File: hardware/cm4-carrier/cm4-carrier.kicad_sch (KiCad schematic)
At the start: 0 parts

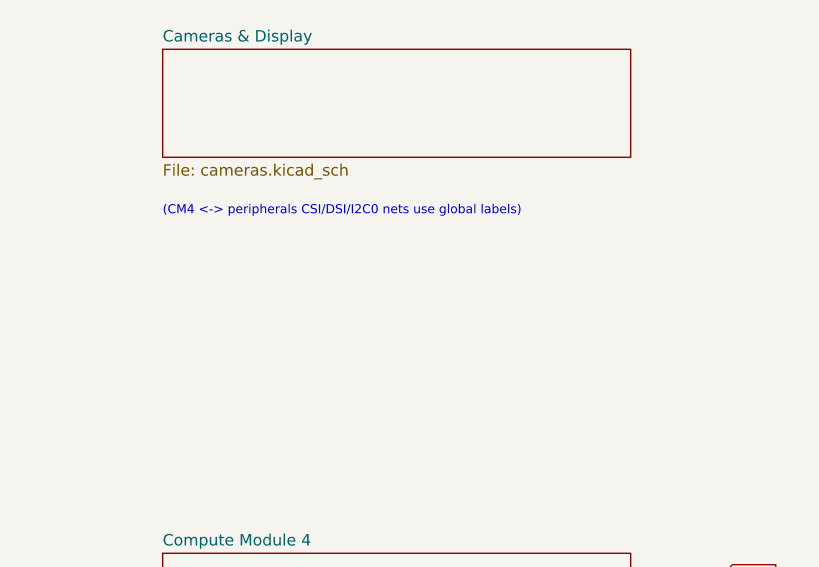
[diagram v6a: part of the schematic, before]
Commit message: Add microSD boot (CM4 Lite) and CM4 bring-up controls
Add a boot_sd.kicad_sch sub-sheet with a microSD socket and the CM4 module
bring-up controls, so a CM4 Lite (no eMMC) can boot from card:

- microSD socket (J8, Hirose DM3D-SF) wired to the CM4 SD interface
  (SD_CLK/SD_CMD/SD_DAT0-3) with CMD/DAT pull-ups and a card-detect pull-up.
- SD 3.3V is gated by a high-side load switch (Q2 P-FET + Q3 N-FET) driven by
  the CM4's SD_PWR_ON (active high), with the card rail decoupled (C16/C17).
  SD_VDD_Override is defaulted low (3.3V card).
- Bring-up controls: GLOBAL_EN (power/enable, SW1), RUN_PG (run/reset, SW2)
  and nRPIBOOT (USB/rpiboot, SW3), each with a pull-up and momentary button;
  nEXTRST pulled up; power/activity LEDs (D3/D4) on PI_LED_nPWR / PI_LED_ACT.

The CM4 sheet now exports the SD interface and the GLOBAL_EN/RUN_PG/nRPIBOOT/
nEXTRST/PI_LED/SD_PWR_ON/SD_VDD_Override pins (from J1) as global nets; the
boot sheet consumes them. Pin directions were taken from the CM4 pin map;
microSD/SOT-23/tact-switch footprints from KiCad libraries.

Root gains a (pinless) Boot sheet box (page 8, now 7 sub-sheets). README/BOM
updated. No format change (KiCad 10, 20260306).

Co-Authored-By: Claude Opus 4.8 <noreply@anthropic.com>
Claude-Session: https://claude.ai/code/session_015B7X7FE461jFSRaiTFdnFt
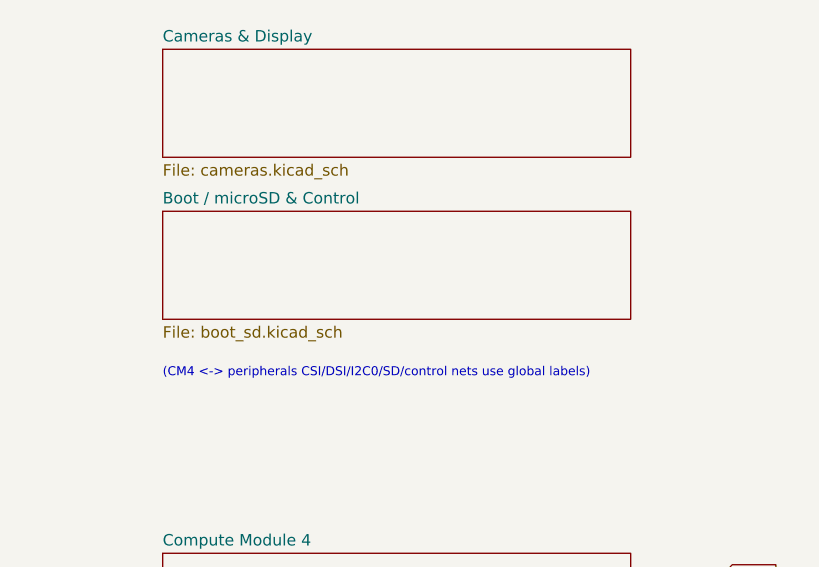
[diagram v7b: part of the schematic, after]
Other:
- added sheet Boot / microSD & Control (boot_sd.kicad_sch)
- note added: "(CM4 <-> peripherals CSI/DSI/I2C0/SD/control nets use global labels)"
- note removed: "(CM4 <-> peripherals CSI/DSI/I2C0 nets use global labels)"
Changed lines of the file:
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@@
 		(instances
 			(project "cm4-carrier"
-				(path "/68164e39-daeb-4d86-8c19-ac7cd09b1aca"
+				(path "/c714cb6b-329f-4585-a26c-317da9f46ca5"
 					(page "6"))))
 	)
@@
 		(instances
 			(project "cm4-carrier"
-				(path "/68164e39-daeb-4d86-8c19-ac7cd09b1aca"
+				(path "/c714cb6b-329f-4585-a26c-317da9f46ca5"
 					(page "2"))))
 	)
@@
 		(instances
 			(project "cm4-carrier"
-				(path "/68164e39-daeb-4d86-8c19-ac7cd09b1aca"
+				(path "/c714cb6b-329f-4585-a26c-317da9f46ca5"
 					(page "3"))))
 	)
@@
 		(instances
 			(project "cm4-carrier"
-				(path "/68164e39-daeb-4d86-8c19-ac7cd09b1aca"
+				(path "/c714cb6b-329f-4585-a26c-317da9f46ca5"
 					(page "4"))))
 	)
@@
 		(instances
 			(project "cm4-carrier"
-				(path "/68164e39-daeb-4d86-8c19-ac7cd09b1aca"
+				(path "/c714cb6b-329f-4585-a26c-317da9f46ca5"
 					(page "5"))))
 	)
@@
 		(instances
 			(project "cm4-carrier"
-				(path "/68164e39-daeb-4d86-8c19-ac7cd09b1aca"
+				(path "/c714cb6b-329f-4585-a26c-317da9f46ca5"
 					(page "7"))))
 	)
-	(text "(CM4 <-> peripherals CSI/DSI/I2C0 nets use global labels)" (at 155.00 58.00 0)
+	(sheet (at 155.00 58.00) (size 52.00 12.00)
+		(exclude_from_sim no) (in_bom yes) (on_board yes) (dnp no)
+		(fields_autoplaced yes)
+		(stroke (width 0.1524) (type solid))
+		(fill (color 0 0 0 0.0000))
+		(property "Sheetname" "Boot / microSD & Control" (at 155.00 57.29 0)
+			(effects (font (size 1.27 1.27)) (justify left bottom)))
+		(property "Sheetfile" "boot_sd.kicad_sch" (at 155.00 70.71 0)
+			(effects (font (size 1.27 1.27)) (justify left top)))
+		(instances
+			(project "cm4-carrier"
+				(path "/c714cb6b-329f-4585-a26c-317da9f46ca5"
+					(page "8"))))
+	)
+	(text "(CM4 <-> peripherals CSI/DSI/I2C0/SD/control nets use global labels)" (at 155.00 76.00 0)
 		(effects (font (size 1.0 1.0)) (justify left))
 )

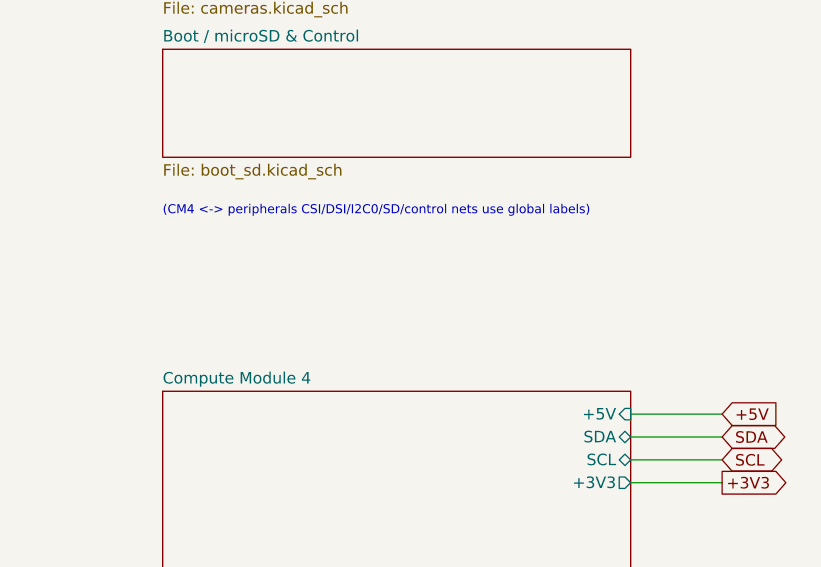
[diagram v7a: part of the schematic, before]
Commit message: Add stereo I2S audio (2x ICS-43434 mics + 2x MAX98357A amps)
Add an audio.kicad_sch sub-sheet with stereo microphone capture and stereo
speaker output over the CM4's I2S peripheral:

- 2x ICS-43434 I2S MEMS mics (U8 Left = LR->GND, U9 Right = LR->VDD) sharing
  the I2S RX bus, powered at 3.3V, with decoupling.
- 2x MAX98357A I2S class-D amps (U10 Left, U11 Right) on the I2S TX bus,
  powered at 5V; channel selected by the SD_MODE resistor divider, GAIN_SLOT
  set via 100k, VDD bulk/decoupling. Filterless BTL outputs go straight to the
  speaker connector.
- 4-pin 1.25mm (JST GH) speaker connector J9 = SPK_L+/L-/R+/R-.

The CM4 sheet exports the I2S bus (GPIO18=BCLK, GPIO19=LRCLK, GPIO20=PCM_DIN,
GPIO21=PCM_DOUT) as global nets I2S_CLK/FS/DIN/DOUT; the audio sheet consumes
them. Both mics+amps share BCLK/LRCLK; mics drive DIN, amps receive DOUT.

Pinouts: ICS-43434 from KiCad Sensor_Audio; MAX98357A (TQFN-16) from KiCad
symbol MR !3846; JST GH 4-pin footprint from KiCad. Root gains a (pinless)
Stereo Audio box (page 9, now 8 sub-sheets). README/BOM updated. No format
change (KiCad 10, 20260306).

Co-Authored-By: Claude Opus 4.8 <noreply@anthropic.com>
Claude-Session: https://claude.ai/code/session_015B7X7FE461jFSRaiTFdnFt
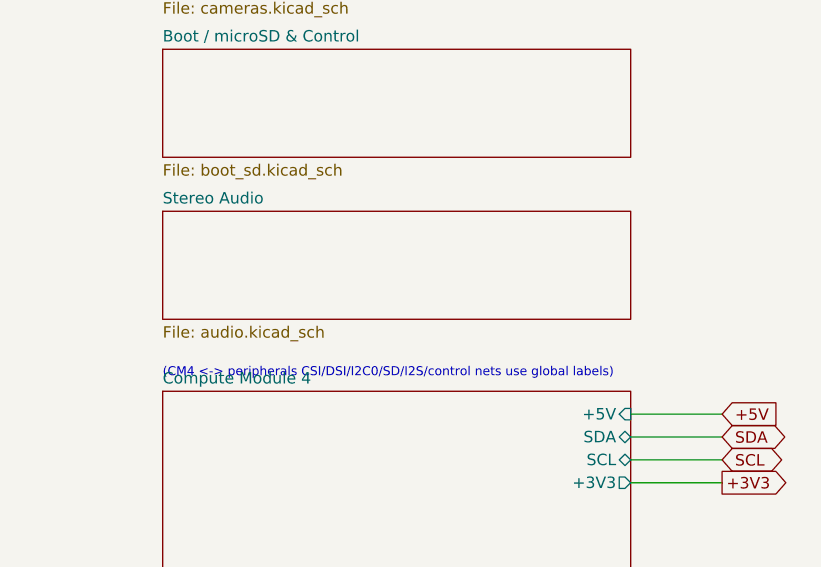
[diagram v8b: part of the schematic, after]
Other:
- added sheet Stereo Audio (audio.kicad_sch)
- note added: "(CM4 <-> peripherals CSI/DSI/I2C0/SD/I2S/control nets use global labels)"
- note removed: "(CM4 <-> peripherals CSI/DSI/I2C0/SD/control nets use global labels)"
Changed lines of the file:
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@@
 		(instances
 			(project "cm4-carrier"
-				(path "/c714cb6b-329f-4585-a26c-317da9f46ca5"
+				(path "/4125949c-82e9-47d9-b22c-a43e01f07343"
 					(page "6"))))
 	)
@@
 		(instances
 			(project "cm4-carrier"
-				(path "/c714cb6b-329f-4585-a26c-317da9f46ca5"
+				(path "/4125949c-82e9-47d9-b22c-a43e01f07343"
 					(page "2"))))
 	)
@@
 		(instances
 			(project "cm4-carrier"
-				(path "/c714cb6b-329f-4585-a26c-317da9f46ca5"
+				(path "/4125949c-82e9-47d9-b22c-a43e01f07343"
 					(page "3"))))
 	)
@@
 		(instances
 			(project "cm4-carrier"
-				(path "/c714cb6b-329f-4585-a26c-317da9f46ca5"
+				(path "/4125949c-82e9-47d9-b22c-a43e01f07343"
 					(page "4"))))
 	)
@@
 		(instances
 			(project "cm4-carrier"
-				(path "/c714cb6b-329f-4585-a26c-317da9f46ca5"
+				(path "/4125949c-82e9-47d9-b22c-a43e01f07343"
 					(page "5"))))
 	)
@@
 		(instances
 			(project "cm4-carrier"
-				(path "/c714cb6b-329f-4585-a26c-317da9f46ca5"
+				(path "/4125949c-82e9-47d9-b22c-a43e01f07343"
 					(page "7"))))
 	)
@@
 		(instances
 			(project "cm4-carrier"
-				(path "/c714cb6b-329f-4585-a26c-317da9f46ca5"
+				(path "/4125949c-82e9-47d9-b22c-a43e01f07343"
 					(page "8"))))
 	)
-	(text "(CM4 <-> peripherals CSI/DSI/I2C0/SD/control nets use global labels)" (at 155.00 76.00 0)
+	(sheet (at 155.00 76.00) (size 52.00 12.00)
+		(exclude_from_sim no) (in_bom yes) (on_board yes) (dnp no)
+		(fields_autoplaced yes)
+		(stroke (width 0.1524) (type solid))
+		(fill (color 0 0 0 0.0000))
+		(property "Sheetname" "Stereo Audio" (at 155.00 75.29 0)
+			(effects (font (size 1.27 1.27)) (justify left bottom)))
+		(property "Sheetfile" "audio.kicad_sch" (at 155.00 88.71 0)
+			(effects (font (size 1.27 1.27)) (justify left top)))
+		(instances
+			(project "cm4-carrier"
+				(path "/4125949c-82e9-47d9-b22c-a43e01f07343"
+					(page "9"))))
+	)
+	(text "(CM4 <-> peripherals CSI/DSI/I2C0/SD/I2S/control nets use global labels)" (at 155.00 94.00 0)
 		(effects (font (size 1.0 1.0)) (justify left))
 )
